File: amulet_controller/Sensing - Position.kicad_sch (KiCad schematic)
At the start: 7 parts, among them U10 AS5048B, U9 AS5047P

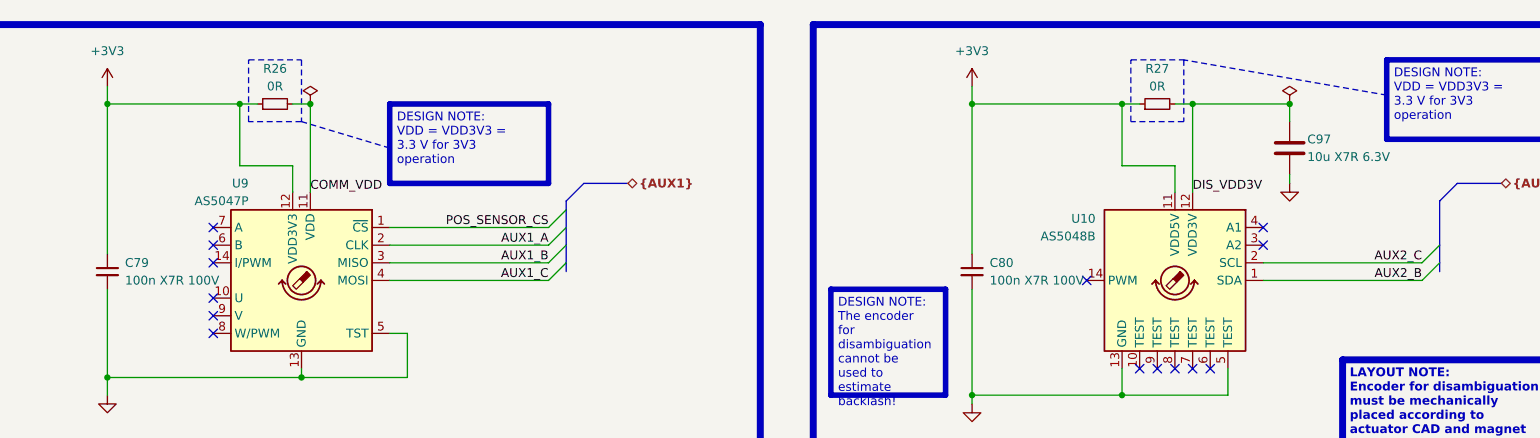
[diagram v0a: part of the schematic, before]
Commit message: filled in fields for bom, replaced inexisting components. Need to replace LEDs
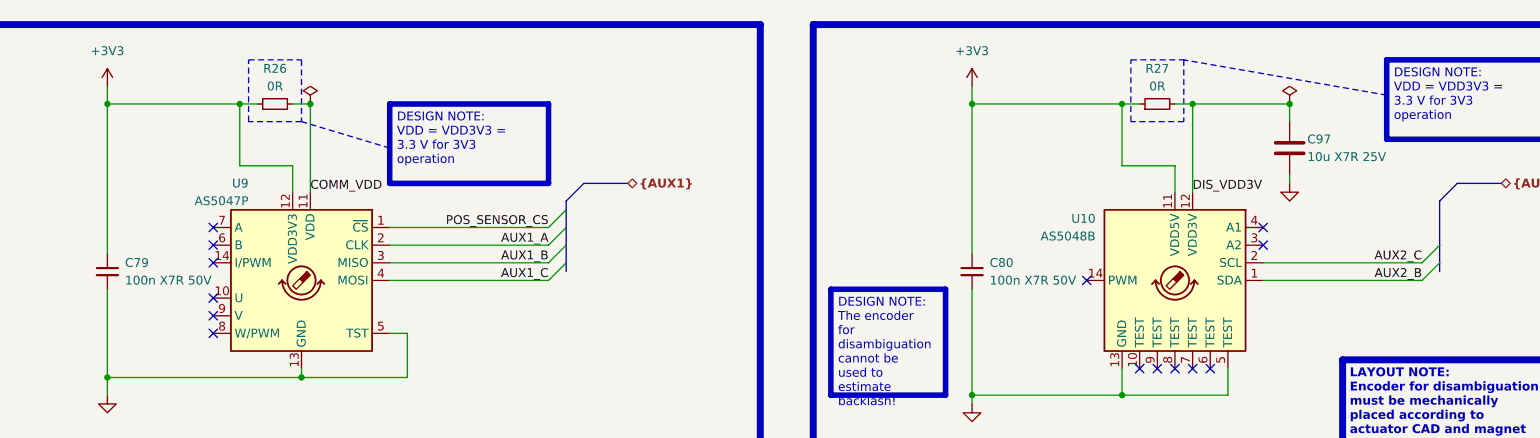
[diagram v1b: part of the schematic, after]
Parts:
- C79, C80: value 100n X7R 100V -> 100n X7R 50V; Manufacturer (none) -> Murata Electronics; Manufacturer Part Number (none) -> GCM155R71H104KE02J; Supplier 1 (none) -> Digikey; Supplier Part Number 1 (none) -> 490-14514-1-ND
- C97: value 10u X7R 6.3V -> 10u X7R 25V; Manufacturer (none) -> Murata Electronics; Manufacturer Part Number (none) -> GRM21BZ71E106KE15L; Supplier 1 (none) -> Digikey; Supplier Part Number 1 (none) -> 490-GRM21BZ71E106KE15LCT-ND
- R26, R27: Manufacturer (none) -> Panasonic Electronic Components; Manufacturer Part Number (none) -> ERJ-2GE0R00X; Supplier 1 (none) -> Digikey; Supplier Part Number 1 (none) -> P0.0JCT-ND
- U10: Manufacturer (none) -> ams-OSRAM USA INC.; Manufacturer Part Number (none) -> AS5048B-HTSP-500; Supplier 1 (none) -> Digikey; Supplier Part Number 1 (none) -> AS5048B-HTSP-500CT-ND
- U9: Manufacturer (none) -> ams-OSRAM USA INC.; Manufacturer Part Number (none) -> AS5047P-ATSM; Supplier 1 (none) -> Digikey; Supplier Part Number 1 (none) -> AS5047P-ATSMCT-ND

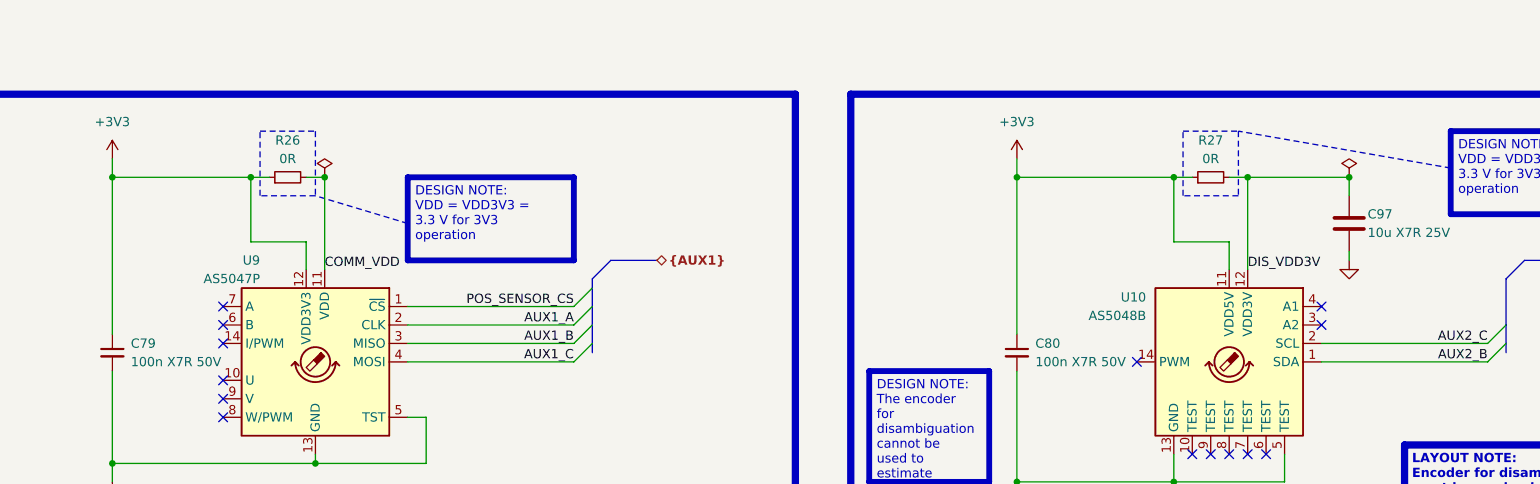
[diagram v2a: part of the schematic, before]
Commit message: finalized pcb. TODO: add clean BOM and KiBot integration
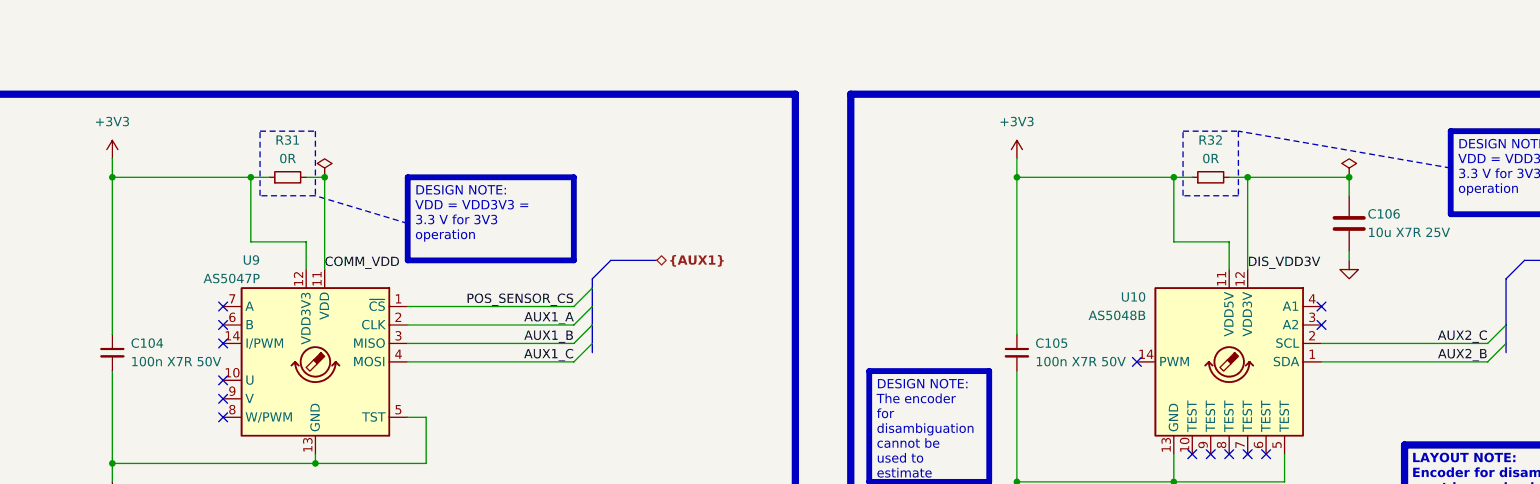
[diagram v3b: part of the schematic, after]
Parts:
- renumbered C79 to C104, C80 to C105, C97 to C106, R26 to R31, R27 to R32
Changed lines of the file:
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@@
   (symbol (lib_id "Device:C_Small") (at 50.8 92.71 0) (unit 1)
     (in_bom yes) (on_board yes) (dnp no) (fields_autoplaced)
-    (property "Reference" "C79" (at 53.34 91.4463 0)
+    (property "Reference" "C104" (at 53.34 91.4463 0)
       (effects (font (size 1.27 1.27)) (justify left))
     )
@@
       (project "amulet_controller"
         (path "/0650c7a8-acba-429c-9f8e-eec0baf0bc1c/fede4c36-00cc-4d3d-b71c-5243ba232202/9d5dddd8-2f86-4eaa-a196-d6c612b385ec"
-          (reference "C79") (unit 1)
+          (reference "C104") (unit 1)
         )
       )
@@
   (symbol (lib_id "Device:R_Small") (at 74.93 68.58 90) (unit 1)
     (in_bom yes) (on_board yes) (dnp no) (fields_autoplaced)
-    (property "Reference" "R26" (at 74.93 63.5 90)
+    (property "Reference" "R31" (at 74.93 63.5 90)
       (effects (font (size 1.27 1.27)))
     )
@@
       (project "amulet_controller"
         (path "/0650c7a8-acba-429c-9f8e-eec0baf0bc1c/fede4c36-00cc-4d3d-b71c-5243ba232202/9d5dddd8-2f86-4eaa-a196-d6c612b385ec"
-          (reference "R26") (unit 1)
+          (reference "R31") (unit 1)
         )
       )
@@
   (symbol (lib_id "Device:C") (at 220.98 74.93 0) (unit 1)
     (in_bom yes) (on_board yes) (dnp no)
-    (property "Reference" "C97" (at 223.52 73.66 0)
+    (property "Reference" "C106" (at 223.52 73.66 0)
       (effects (font (size 1.27 1.27)) (justify left))
     )
@@
       (project "amulet_controller"
         (path "/0650c7a8-acba-429c-9f8e-eec0baf0bc1c/fede4c36-00cc-4d3d-b71c-5243ba232202/9d5dddd8-2f86-4eaa-a196-d6c612b385ec"
-          (reference "C97") (unit 1)
+          (reference "C106") (unit 1)
         )
       )
@@
   (symbol (lib_id "power:+3V3") (at 50.8 66.04 0) (unit 1)
     (in_bom yes) (on_board yes) (dnp no) (fields_autoplaced)
-    (property "Reference" "#PWR045" (at 50.8 69.85 0)
+    (property "Reference" "#PWR046" (at 50.8 69.85 0)
       (effects (font (size 1.27 1.27)) hide)
     )
@@
       (project "amulet_controller"
         (path "/0650c7a8-acba-429c-9f8e-eec0baf0bc1c/fede4c36-00cc-4d3d-b71c-5243ba232202/9d5dddd8-2f86-4eaa-a196-d6c612b385ec"
-          (reference "#PWR045") (unit 1)
+          (reference "#PWR046") (unit 1)
         )
       )
@@
   (symbol (lib_id "power:PWR_FLAG") (at 220.98 68.58 0) (unit 1)
     (in_bom yes) (on_board yes) (dnp no) (fields_autoplaced)
-    (property "Reference" "#FLG06" (at 220.98 66.675 0)
+    (property "Reference" "#FLG010" (at 220.98 66.675 0)
       (effects (font (size 1.27 1.27)) hide)
     )
@@
       (project "amulet_controller"
         (path "/0650c7a8-acba-429c-9f8e-eec0baf0bc1c/fede4c36-00cc-4d3d-b71c-5243ba232202/9d5dddd8-2f86-4eaa-a196-d6c612b385ec"
-          (reference "#FLG06") (unit 1)
+          (reference "#FLG010") (unit 1)
         )
       )
@@
   (symbol (lib_id "power:GND") (at 50.8 110.49 0) (unit 1)
     (in_bom yes) (on_board yes) (dnp no) (fields_autoplaced)
-    (property "Reference" "#PWR046" (at 50.8 116.84 0)
+    (property "Reference" "#PWR047" (at 50.8 116.84 0)
       (effects (font (size 1.27 1.27)) hide)
     )
@@
       (project "amulet_controller"
         (path "/0650c7a8-acba-429c-9f8e-eec0baf0bc1c/fede4c36-00cc-4d3d-b71c-5243ba232202/9d5dddd8-2f86-4eaa-a196-d6c612b385ec"
-          (reference "#PWR046") (unit 1)
+          (reference "#PWR047") (unit 1)
         )
       )
@@
   (symbol (lib_id "power:GND") (at 175.26 111.76 0) (unit 1)
     (in_bom yes) (on_board yes) (dnp no) (fields_autoplaced)
-    (property "Reference" "#PWR048" (at 175.26 118.11 0)
+    (property "Reference" "#PWR049" (at 175.26 118.11 0)
       (effects (font (size 1.27 1.27)) hide)
     )
@@
       (project "amulet_controller"
         (path "/0650c7a8-acba-429c-9f8e-eec0baf0bc1c/fede4c36-00cc-4d3d-b71c-5243ba232202/9d5dddd8-2f86-4eaa-a196-d6c612b385ec"
-          (reference "#PWR048") (unit 1)
+          (reference "#PWR049") (unit 1)
         )
       )
@@
   (symbol (lib_id "Device:R_Small") (at 201.93 68.58 90) (unit 1)
     (in_bom yes) (on_board yes) (dnp no) (fields_autoplaced)
-    (property "Reference" "R27" (at 201.93 63.5 90)
+    (property "Reference" "R32" (at 201.93 63.5 90)
       (effects (font (size 1.27 1.27)))
     )
@@
       (project "amulet_controller"
         (path "/0650c7a8-acba-429c-9f8e-eec0baf0bc1c/fede4c36-00cc-4d3d-b71c-5243ba232202/9d5dddd8-2f86-4eaa-a196-d6c612b385ec"
-          (reference "R27") (unit 1)
+          (reference "R32") (unit 1)
         )
       )
@@
   (symbol (lib_id "power:+3V3") (at 175.26 66.04 0) (unit 1)
     (in_bom yes) (on_board yes) (dnp no) (fields_autoplaced)
-    (property "Reference" "#PWR047" (at 175.26 69.85 0)
+    (property "Reference" "#PWR048" (at 175.26 69.85 0)
       (effects (font (size 1.27 1.27)) hide)
     )
@@
       (project "amulet_controller"
         (path "/0650c7a8-acba-429c-9f8e-eec0baf0bc1c/fede4c36-00cc-4d3d-b71c-5243ba232202/9d5dddd8-2f86-4eaa-a196-d6c612b385ec"
-          (reference "#PWR047") (unit 1)
+          (reference "#PWR048") (unit 1)
         )
       )
@@
   (symbol (lib_id "power:GND") (at 220.98 80.01 0) (unit 1)
     (in_bom yes) (on_board yes) (dnp no) (fields_autoplaced)
-    (property "Reference" "#PWR049" (at 220.98 86.36 0)
+    (property "Reference" "#PWR050" (at 220.98 86.36 0)
       (effects (font (size 1.27 1.27)) hide)
     )
@@
       (project "amulet_controller"
         (path "/0650c7a8-acba-429c-9f8e-eec0baf0bc1c/fede4c36-00cc-4d3d-b71c-5243ba232202/9d5dddd8-2f86-4eaa-a196-d6c612b385ec"
-          (reference "#PWR049") (unit 1)
+          (reference "#PWR050") (unit 1)
         )
       )
@@
   (symbol (lib_id "power:PWR_FLAG") (at 80.01 68.58 0) (unit 1)
     (in_bom yes) (on_board yes) (dnp no) (fields_autoplaced)
-    (property "Reference" "#FLG05" (at 80.01 66.675 0)
+    (property "Reference" "#FLG09" (at 80.01 66.675 0)
       (effects (font (size 1.27 1.27)) hide)
     )
@@
       (project "amulet_controller"
         (path "/0650c7a8-acba-429c-9f8e-eec0baf0bc1c/fede4c36-00cc-4d3d-b71c-5243ba232202/9d5dddd8-2f86-4eaa-a196-d6c612b385ec"
-          (reference "#FLG05") (unit 1)
+          (reference "#FLG09") (unit 1)
         )
       )
@@
   (symbol (lib_id "Device:C_Small") (at 175.26 92.71 0) (unit 1)
     (in_bom yes) (on_board yes) (dnp no) (fields_autoplaced)
-    (property "Reference" "C80" (at 177.8 91.4463 0)
+    (property "Reference" "C105" (at 177.8 91.4463 0)
       (effects (font (size 1.27 1.27)) (justify left))
     )
@@
       (project "amulet_controller"
         (path "/0650c7a8-acba-429c-9f8e-eec0baf0bc1c/fede4c36-00cc-4d3d-b71c-5243ba232202/9d5dddd8-2f86-4eaa-a196-d6c612b385ec"
-          (reference "C80") (unit 1)
-        )
-      )
+          (reference "C105") (unit 1)
+        )
+      )

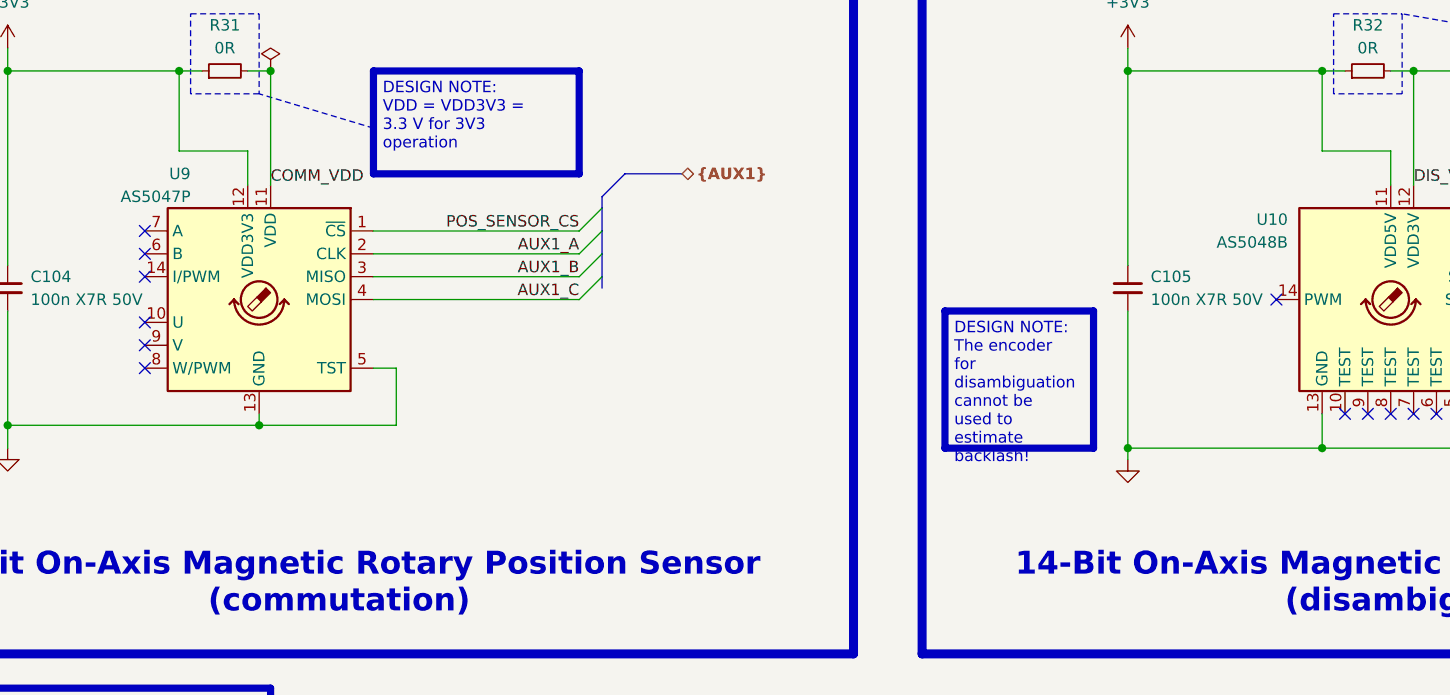
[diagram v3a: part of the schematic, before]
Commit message: corrected pcb according to reviews on reddit
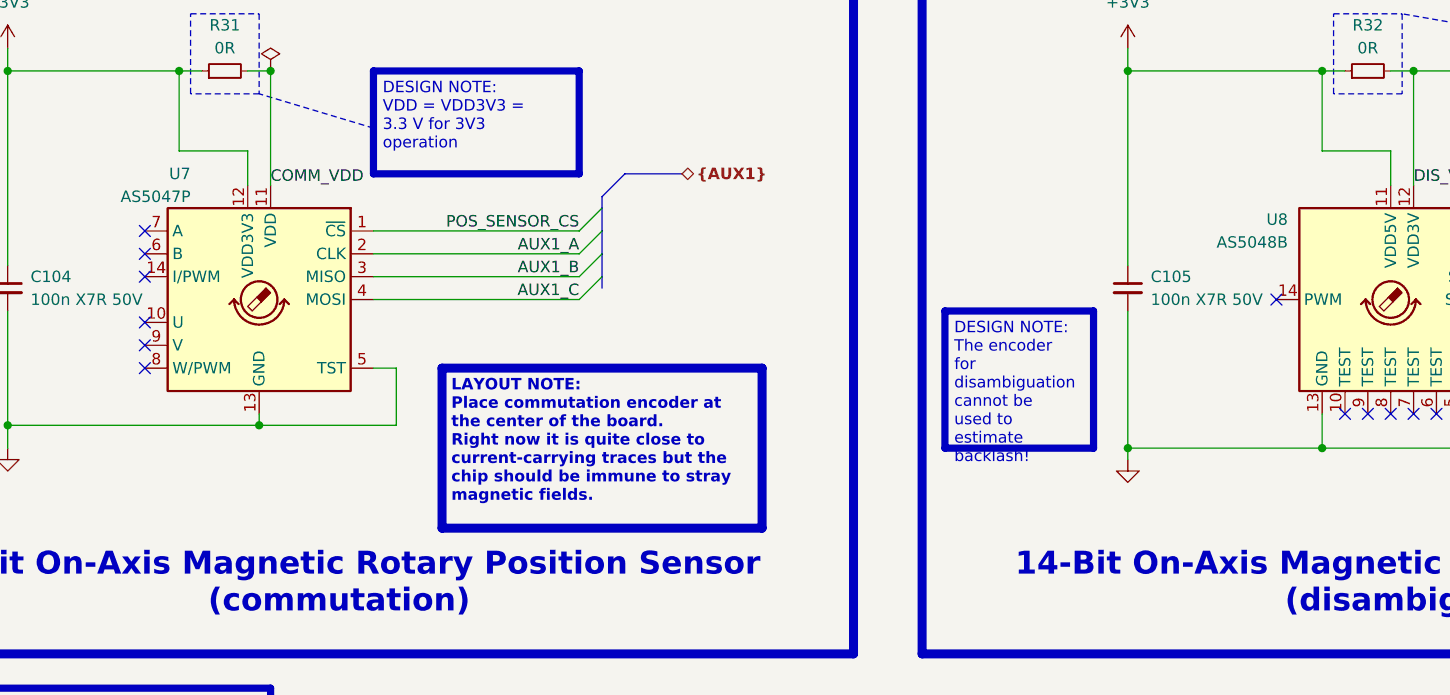
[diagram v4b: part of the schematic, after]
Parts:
- renumbered U9 to U7, U10 to U8
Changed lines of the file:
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@@
     (effects (font (face "Arial") (size 1.27 1.27) (color 0 0 0 1)) (justify left top))
+  )
+  (text_box "LAYOUT NOTE:\nPlace commutation encoder at the center of the board. \nRight now it is quite close to current-carrying traces but the chip should be immune to stray magnetic fields."
+    (at 99.06 101.6 0) (size 35.56 17.78)
+    (stroke (width 1) (type solid) (color 0 0 255 1))
+    (fill (type none))
+    (effects (font (face "Arial") (size 1.27 1.27) (thickness 0.4) bold (color 0 0 255 1)) (justify left top))
   )
   (text_box "DESIGN NOTE:\nAS5047P senses magnet mounted on planetary sun gear, for commutation.\nAS5048B senses magnet mounted on shaft with same reduction factor as planetary gearbox for disambiguation."
@@
   (symbol (lib_id "power:+3V3") (at 50.8 66.04 0) (unit 1)
     (in_bom yes) (on_board yes) (dnp no) (fields_autoplaced)
-    (property "Reference" "#PWR046" (at 50.8 69.85 0)
+    (property "Reference" "#PWR047" (at 50.8 69.85 0)
       (effects (font (size 1.27 1.27)) hide)
     )
@@
       (project "amulet_controller"
         (path "/0650c7a8-acba-429c-9f8e-eec0baf0bc1c/fede4c36-00cc-4d3d-b71c-5243ba232202/9d5dddd8-2f86-4eaa-a196-d6c612b385ec"
-          (reference "#PWR046") (unit 1)
+          (reference "#PWR047") (unit 1)
         )
       )
@@
   (symbol (lib_id "power:GND") (at 50.8 110.49 0) (unit 1)
     (in_bom yes) (on_board yes) (dnp no) (fields_autoplaced)
-    (property "Reference" "#PWR047" (at 50.8 116.84 0)
+    (property "Reference" "#PWR048" (at 50.8 116.84 0)
       (effects (font (size 1.27 1.27)) hide)
     )
@@
       (project "amulet_controller"
         (path "/0650c7a8-acba-429c-9f8e-eec0baf0bc1c/fede4c36-00cc-4d3d-b71c-5243ba232202/9d5dddd8-2f86-4eaa-a196-d6c612b385ec"
-          (reference "#PWR047") (unit 1)
+          (reference "#PWR048") (unit 1)
         )
       )
@@
   (symbol (lib_id "0_sensor:AS5047P") (at 78.74 93.98 0) (mirror y) (unit 1)
     (in_bom yes) (on_board yes) (dnp no)
-    (property "Reference" "U9" (at 71.12 80.01 0)
+    (property "Reference" "U7" (at 71.12 80.01 0)
       (effects (font (size 1.27 1.27)) (justify left))
     )
@@
       (project "amulet_controller"
         (path "/0650c7a8-acba-429c-9f8e-eec0baf0bc1c/fede4c36-00cc-4d3d-b71c-5243ba232202/9d5dddd8-2f86-4eaa-a196-d6c612b385ec"
-          (reference "U9") (unit 1)
+          (reference "U7") (unit 1)
         )
       )
@@
   (symbol (lib_id "power:GND") (at 175.26 111.76 0) (unit 1)
     (in_bom yes) (on_board yes) (dnp no) (fields_autoplaced)
-    (property "Reference" "#PWR049" (at 175.26 118.11 0)
+    (property "Reference" "#PWR050" (at 175.26 118.11 0)
       (effects (font (size 1.27 1.27)) hide)
     )
@@
       (project "amulet_controller"
         (path "/0650c7a8-acba-429c-9f8e-eec0baf0bc1c/fede4c36-00cc-4d3d-b71c-5243ba232202/9d5dddd8-2f86-4eaa-a196-d6c612b385ec"
-          (reference "#PWR049") (unit 1)
+          (reference "#PWR050") (unit 1)
         )
       )
@@
   (symbol (lib_id "Sensor_Magnetic:AS5048B") (at 204.47 93.98 0) (mirror y) (unit 1)
     (in_bom yes) (on_board yes) (dnp no)
-    (property "Reference" "U10" (at 193.04 85.09 0)
+    (property "Reference" "U8" (at 193.04 85.09 0)
       (effects (font (size 1.27 1.27)) (justify left))
     )
@@
       (project "amulet_controller"
         (path "/0650c7a8-acba-429c-9f8e-eec0baf0bc1c/fede4c36-00cc-4d3d-b71c-5243ba232202/9d5dddd8-2f86-4eaa-a196-d6c612b385ec"
-          (reference "U10") (unit 1)
+          (reference "U8") (unit 1)
         )
       )
@@
   (symbol (lib_id "power:+3V3") (at 175.26 66.04 0) (unit 1)
     (in_bom yes) (on_board yes) (dnp no) (fields_autoplaced)
-    (property "Reference" "#PWR048" (at 175.26 69.85 0)
+    (property "Reference" "#PWR049" (at 175.26 69.85 0)
       (effects (font (size 1.27 1.27)) hide)
     )
@@
       (project "amulet_controller"
         (path "/0650c7a8-acba-429c-9f8e-eec0baf0bc1c/fede4c36-00cc-4d3d-b71c-5243ba232202/9d5dddd8-2f86-4eaa-a196-d6c612b385ec"
-          (reference "#PWR048") (unit 1)
+          (reference "#PWR049") (unit 1)
         )
       )
@@
   (symbol (lib_id "power:GND") (at 220.98 80.01 0) (unit 1)
     (in_bom yes) (on_board yes) (dnp no) (fields_autoplaced)
-    (property "Reference" "#PWR050" (at 220.98 86.36 0)
+    (property "Reference" "#PWR051" (at 220.98 86.36 0)
       (effects (font (size 1.27 1.27)) hide)
     )
@@
       (project "amulet_controller"
         (path "/0650c7a8-acba-429c-9f8e-eec0baf0bc1c/fede4c36-00cc-4d3d-b71c-5243ba232202/9d5dddd8-2f86-4eaa-a196-d6c612b385ec"
-          (reference "#PWR050") (unit 1)
-        )
-      )
+          (reference "#PWR051") (unit 1)
+        )
+      )
